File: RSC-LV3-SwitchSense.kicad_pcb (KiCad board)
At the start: 2 copper layers, 138 parts, among them J10 Molex 43045-0400, J11 Molex 43045-0400, J12 Molex 43045-0400, J13 Molex 43045-0400, J14 Molex 43045-0400, J15 Molex 43045-0400, J16 Molex 43045-0400, J17 Molex 43045-0400, J18 Molex 43045-0400, J2 USB_C_Receptacle_USB2.0_16P, J3 Conn_01x01, J5 Molex 43650-0500, J6 Molex 43650-0500, J8 FTSH-105-01-L-DV-K-A, J9 Molex 43045-0400, Q10 AO3400A, Q11 AO3400A, Q2 AO3400A, Q3 AO3400A, Q4 AO3400A, Q5 AO3400A, Q6 AO3400A, Q7 AO3400A, Q8 AO3400A, Q9 AO3400A, U1 STM32G0B1CBTx, U2 TJA1051T-3, U3 TPS54302, U5 TLV74033PDBVR, Y1 Crystal_GND24

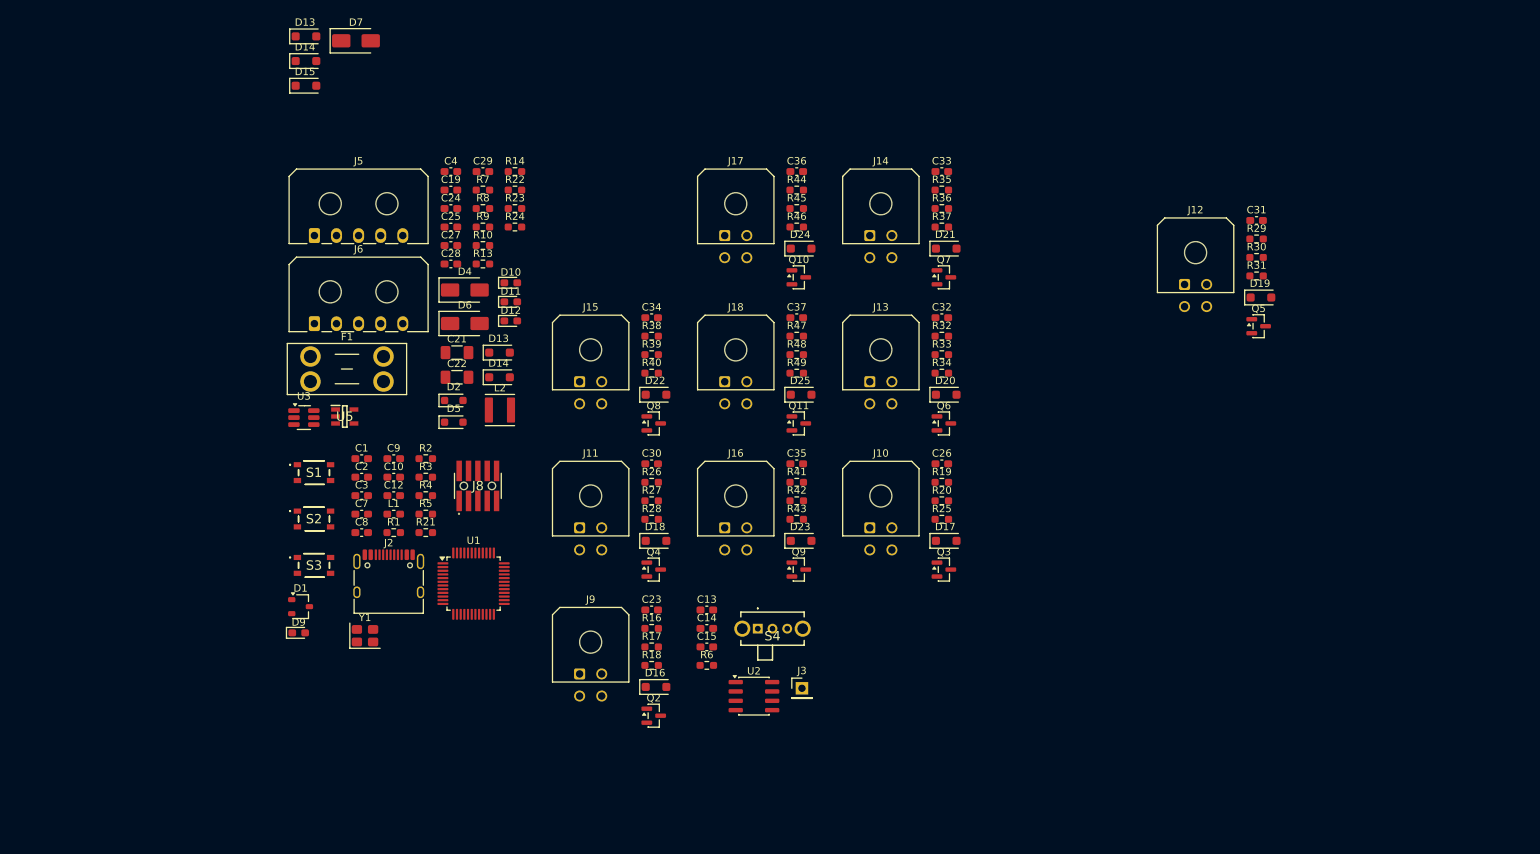
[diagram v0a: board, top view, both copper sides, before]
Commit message: updated pinout, begin layout
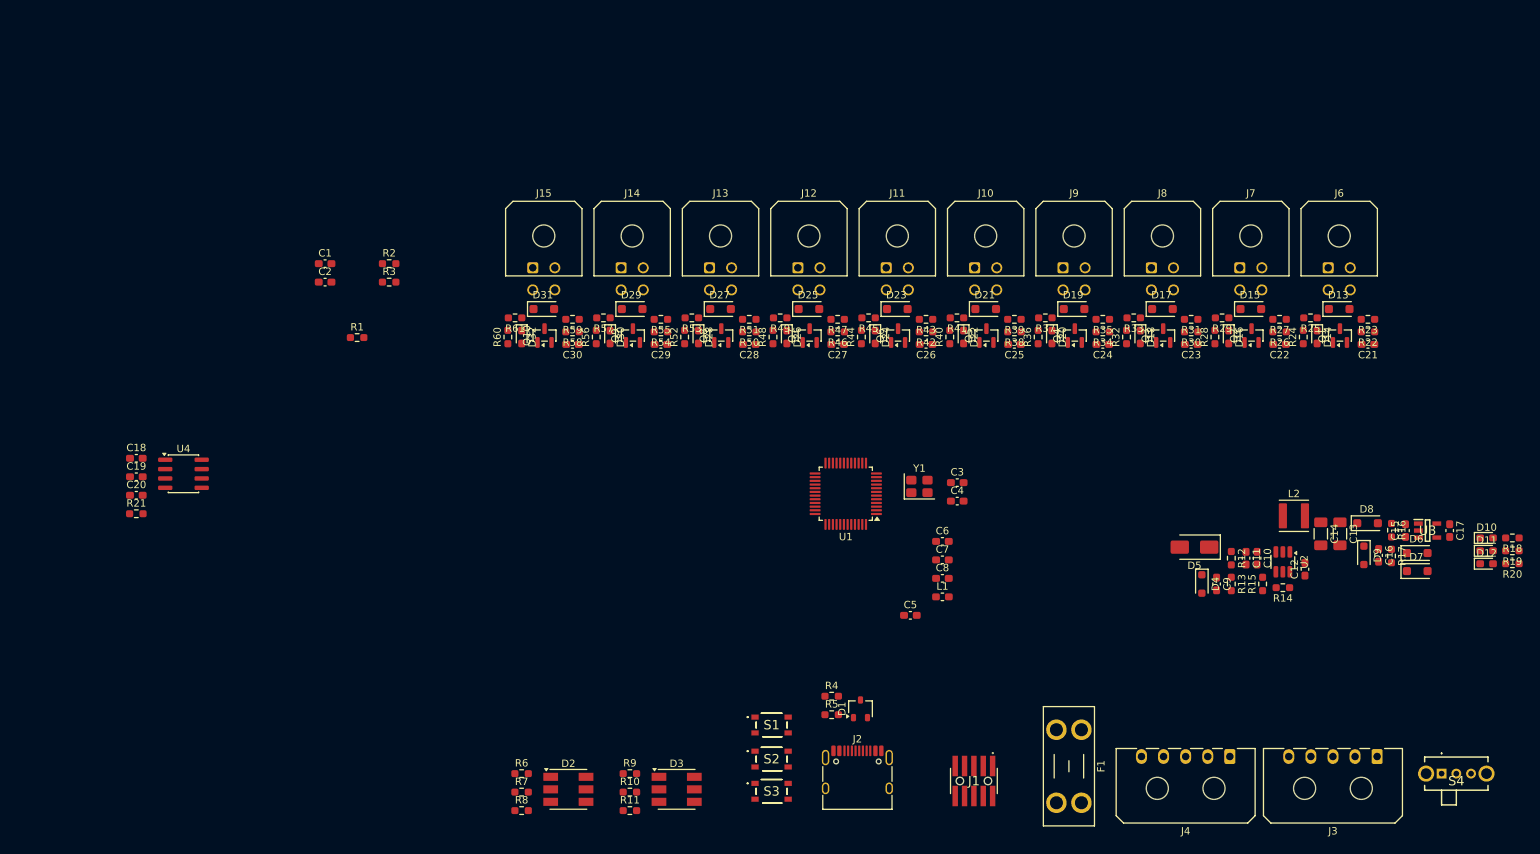
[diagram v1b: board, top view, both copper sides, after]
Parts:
- removed the C21 at (128.2, 75.8)
- removed the C22 at (128.2, 79.2)
- removed the C24 at (127.4, 56.3)
- removed the C25 at (127.4, 58.8)
- removed the C27 at (127.4, 61.3)
- removed the C28 at (127.4, 63.8)
- removed the C29 at (131.7, 51.3)
- removed the D13 at (134.0, 75.8)
- removed the D13 at (107.7, 32.9)
- removed the D14 at (107.7, 36.2)
- removed the D14 at (134.0, 79.2)
- removed the D15 at (107.7, 39.6)
- removed the J3 at (175.1, 121.4)
- removed the R22 at (136.1, 53.8)
- removed the R23 at (136.1, 56.3)
- removed the R24 at (136.1, 58.8)
- removed U5: TLV74033PDBVR, SamacSys_Parts:SOT95P280X145-5N
- added C11: 2.2u, Capacitor_SMD:C_0603_1608Metric_Pad1.08x0.95mm_HandSolder, F.Cu at (235.3, 103.8)
- added C16: 100n, Capacitor_SMD:C_0603_1608Metric_Pad1.08x0.95mm_HandSolder, F.Cu at (253.3, 103.4)
- added C17: 1u, Capacitor_SMD:C_0603_1608Metric_Pad1.08x0.95mm_HandSolder, F.Cu at (263.0, 100.0)
- added C18: 100n, Capacitor_SMD:C_0603_1608Metric_Pad1.08x0.95mm_HandSolder, F.Cu at (84.7, 90.2)
- added C20: 1u, Capacitor_SMD:C_0603_1608Metric_Pad1.08x0.95mm_HandSolder, F.Cu at (84.7, 95.2)
- added C5: 100n, Capacitor_SMD:C_0603_1608Metric_Pad1.08x0.95mm_HandSolder, F.Cu at (189.8, 111.5)
- added C6: 1u, Capacitor_SMD:C_0603_1608Metric_Pad1.08x0.95mm_HandSolder, F.Cu at (194.1, 101.5)
- added D14: LED, LED_SMD:LED_0603_1608Metric_Pad1.05x0.95mm_HandSolder, F.Cu at (245.0, 73.7)
- added D16: LED, LED_SMD:LED_0603_1608Metric_Pad1.05x0.95mm_HandSolder, F.Cu at (233.0, 73.7)
- added D18: LED, LED_SMD:LED_0603_1608Metric_Pad1.05x0.95mm_HandSolder, F.Cu at (221.0, 73.7)
- added D20: LED, LED_SMD:LED_0603_1608Metric_Pad1.05x0.95mm_HandSolder, F.Cu at (209.0, 73.7)
- added D22: LED, LED_SMD:LED_0603_1608Metric_Pad1.05x0.95mm_HandSolder, F.Cu at (197.0, 73.7)
- added D24: LED, LED_SMD:LED_0603_1608Metric_Pad1.05x0.95mm_HandSolder, F.Cu at (185.0, 73.7)
- added D26: LED, LED_SMD:LED_0603_1608Metric_Pad1.05x0.95mm_HandSolder, F.Cu at (173.0, 73.7)
- added D28: LED, LED_SMD:LED_0603_1608Metric_Pad1.05x0.95mm_HandSolder, F.Cu at (161.0, 73.7)
- added D3: LED_RGB, LED_SMD:LED_RGB_5050-6, F.Cu at (158.0, 135.1)
- added D30: LED, LED_SMD:LED_0603_1608Metric_Pad1.05x0.95mm_HandSolder, F.Cu at (149.0, 73.7)
- added D32: LED, LED_SMD:LED_0603_1608Metric_Pad1.05x0.95mm_HandSolder, F.Cu at (137.0, 73.7)
- added D8: D_Schottky, Diode_SMD:D_SOD-123F, F.Cu at (251.8, 99.0)
- added R11: 120, Resistor_SMD:R_0603_1608Metric_Pad0.98x0.95mm_HandSolder, F.Cu at (151.7, 138.0)
- added R12: 100k, Resistor_SMD:R_0603_1608Metric_Pad0.98x0.95mm_HandSolder, F.Cu at (233.3, 103.8)
- added R15: 12.7k, Resistor_SMD:R_0603_1608Metric_Pad0.98x0.95mm_HandSolder, F.Cu at (237.6, 107.2)
- added R16: 100k, Resistor_SMD:R_0603_1608Metric_Pad0.98x0.95mm_HandSolder, F.Cu at (255.1, 100.0)
- added R17: 100k, Resistor_SMD:R_0603_1608Metric_Pad0.98x0.95mm_HandSolder, F.Cu at (255.1, 103.5)
- added R18: 2.2k, Resistor_SMD:R_0603_1608Metric_Pad0.98x0.95mm_HandSolder, F.Cu at (271.5, 101.0)
- added R19: 470, Resistor_SMD:R_0603_1608Metric_Pad0.98x0.95mm_HandSolder, F.Cu at (271.5, 102.8)
- added R20: 120, Resistor_SMD:R_0603_1608Metric_Pad0.98x0.95mm_HandSolder, F.Cu at (271.5, 104.5)
- added R25: 470, Resistor_SMD:R_0603_1608Metric_Pad0.98x0.95mm_HandSolder, F.Cu at (244.1, 71.1)
- added R29: 470, Resistor_SMD:R_0603_1608Metric_Pad0.98x0.95mm_HandSolder, F.Cu at (232.1, 71.1)
- added R33: 470, Resistor_SMD:R_0603_1608Metric_Pad0.98x0.95mm_HandSolder, F.Cu at (220.1, 71.1)
- added R37: 470, Resistor_SMD:R_0603_1608Metric_Pad0.98x0.95mm_HandSolder, F.Cu at (208.1, 71.1)
- added R41: 470, Resistor_SMD:R_0603_1608Metric_Pad0.98x0.95mm_HandSolder, F.Cu at (196.1, 71.1)
- added R45: 470, Resistor_SMD:R_0603_1608Metric_Pad0.98x0.95mm_HandSolder, F.Cu at (184.1, 71.1)
- added R49: 470, Resistor_SMD:R_0603_1608Metric_Pad0.98x0.95mm_HandSolder, F.Cu at (172.1, 71.1)
- added R53: 470, Resistor_SMD:R_0603_1608Metric_Pad0.98x0.95mm_HandSolder, F.Cu at (160.1, 71.1)
- added R57: 470, Resistor_SMD:R_0603_1608Metric_Pad0.98x0.95mm_HandSolder, F.Cu at (148.1, 71.1)
- added R61: 470, Resistor_SMD:R_0603_1608Metric_Pad0.98x0.95mm_HandSolder, F.Cu at (136.1, 71.1)
- added U4: TJA1051T-3, Package_SO:SOIC-8_3.9x4.9mm_P1.27mm, F.Cu at (91.1, 92.3)
- C1, C2: value 6.8p -> 100n
- C10: value 100n -> 2.2u
- C13: value 100n -> 22u; footprint Capacitor_SMD:C_0603_1608Metric_Pad1.08x0.95mm_HandSolder -> Capacitor_SMD:C_1206_3216Metric_Pad1.33x1.80mm_HandSolder
- C14: value 1u -> 22u; footprint Capacitor_SMD:C_0603_1608Metric_Pad1.08x0.95mm_HandSolder -> Capacitor_SMD:C_1206_3216Metric_Pad1.33x1.80mm_HandSolder
- C15: value 100n -> 1u
- C3, C4: value 100n -> 6.8p
- C8: value 1u -> 100n
- D2: value D_Zener -> LED_RGB; footprint Diode_SMD:D_SOD-323_HandSoldering -> LED_SMD:LED_RGB_5050-6
- D4: value D_Schottky -> D_Zener; footprint Diode_SMD:D_SMA -> Diode_SMD:D_SOD-323_HandSoldering
- D5: value D_Zener -> D_Schottky; footprint Diode_SMD:D_SOD-323_HandSoldering -> Diode_SMD:D_SMA
- D6, D7: footprint Diode_SMD:D_SMA -> Diode_SMD:D_SOD-123F
- D9: value LED -> D_Zener; footprint LED_SMD:LED_0603_1608Metric_Pad1.05x0.95mm_HandSolder -> Diode_SMD:D_SOD-323_HandSoldering
- R10: value 5.1k -> 50
- R13: value 100k -> 5.1k
- R21: value 470 -> 120
- R6: value 120 -> 50
- R7, R9: value 100k -> 50
- R8: value 12.7k -> 120
- U2: value TJA1051T-3 -> TPS54302; footprint Package_SO:SOIC-8_3.9x4.9mm_P1.27mm -> Package_TO_SOT_SMD:SOT-23-6_Handsoldering
- U3: value TPS54302 -> TLV74033PDBVR; footprint Package_TO_SOT_SMD:SOT-23-6_Handsoldering -> SamacSys_Parts:SOT95P280X145-5N
- moved D7 161.1 mm to (258.6, 105.5)
- moved J3 160.7 mm to (253.2, 130.7), turned to 180 degrees
- moved U3 153.3 mm to (260.0, 100.0)
- moved D9 145.0 mm to (251.3, 103.4), turned to -90 degrees
- moved J4 137.5 mm to (233.2, 130.7), turned to 180 degrees
- moved D10 136.9 mm to (268.0, 101.0)
- moved D11 136.7 mm to (268.0, 102.8)
- moved D12 136.5 mm to (268.0, 104.5)
- moved D6 133.0 mm to (258.6, 103.0)
- moved C12 124.1 mm to (243.3, 105.2), turned to 90 degrees
- moved R14 118.6 mm to (240.3, 107.8), turned to 180 degrees
- moved C10 117.7 mm to (236.8, 103.8), turned to -90 degrees
- moved F1 116.3 mm to (213.0, 127.0), turned to -90 degrees
- moved J6 115.6 mm to (246.5, 64.3)
- moved C9 113.0 mm to (231.3, 107.2), turned to -90 degrees
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- renumbered C23 to C21, C26 to C22, C30 to C23, C31 to C24, C32 to C25, C33 to C26, C34 to C27, C35 to C28, C36 to C29, C37 to C30, D16 to D13, D17 to D15, D18 to D17, D20 to D21, D21 to D23, D22 to D25, D23 to D27, D24 to D29, D25 to D31, J8 to J1, J13 to J10, J14 to J11, J15 to J12, J16 to J13, J17 to J14, J18 to J15, J5 to J3, J6 to J4, J9 to J6, J10 to J7, J11 to J8, J12 to J9, Q2 to Q1, Q11 to Q10, Q3 to Q2, Q4 to Q3, Q5 to Q4, Q6 to Q5, Q7 to Q6, Q8 to Q7, Q9 to Q8, Q10 to Q9, R16 to R22, R17 to R23, R18 to R24, R19 to R26, R20 to R27, R25 to R28, R26 to R30, R27 to R31, R28 to R32, R29 to R34, R30 to R35, R31 to R36, R32 to R38, R33 to R39, R34 to R40, R35 to R42, R36 to R43, R37 to R44, R38 to R46, R39 to R47, R40 to R48, R41 to R50, R42 to R51, R43 to R52, R44 to R54, R45 to R55, R46 to R56, R47 to R58, R48 to R59, R49 to R60
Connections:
- C1 pad 1: HSE_IN -> BTN_USR1
- C10 pad 1: NRST -> +12V
- C12 pad 1: BTN_USR1 -> Net-(U2-BOOT)
- C12 pad 2: GND -> Net-(U2-SW)
- C13 pad 1: +5V -> +5V_BUCK
- C14 pad 1: +5V -> +5V_BUCK
- C15 pad 1: +3.3V -> +5V
- C19 pad 1: V_SENSE_12 -> +5V
- C2 pad 1: HSE_OUT -> NRST
- C21 pad 1: /Inputs/SwitchSense 1/SW_SENSE -> IN_1
- C22 pad 1: /Inputs/SwitchSense 2/SW_SENSE -> IN_2
- C23 pad 1: /Inputs/SwitchSense 3/SW_SENSE -> IN_3
- C24 pad 1: /Inputs/SwitchSense 4/SW_SENSE -> IN_4
- C25 pad 1: /Inputs/SwitchSense 5/SW_SENSE -> IN_5
- C26 pad 1: /Inputs/SwitchSense 6/SW_SENSE -> IN_6
- C27 pad 1: /Inputs/SwitchSense 7/SW_SENSE -> IN_7
- C28 pad 1: /Inputs/SwitchSense 8/SW_SENSE -> IN_8
- C29 pad 1: /Inputs/SwitchSense 9/SW_SENSE -> IN_9
- C3 pad 1: +3.3V -> HSE_IN
- C30 pad 1: /Inputs/SwitchSense 10/SW_SENSE -> IN_10
- C4 pad 1: Net-(U3-BOOT) -> HSE_OUT
- C4 pad 2: Net-(U3-SW) -> GND
- C7 pad 1: +3.3V -> +VDDA
- C9 pad 1: +VDDA -> V_SENSE_12
- D2 pad 1: V_SENSE_12 -> Net-(D2-RK)
- D2 pad 2: GND -> Net-(D2-GK)
- D4 pad 1: +5V -> V_SENSE_12
- D4 pad 2: +5V_USB -> GND
- D5 pad 1: V_SENSE_5 -> +12V
- D5 pad 2: GND -> Net-(D5-A)
- D6 pad 2: +5V_BUS -> +5V_USB
- D7 pad 1: Net-(D7-K) -> +5V
- D7 pad 2: +12V -> +5V_BUS
- D9 pad 1: GND -> V_SENSE_5
- D9 pad 2: Net-(D9-A) -> GND
- F1 pad 2: +12V -> Net-(D5-A)
- L2 pad 1: Net-(U3-SW) -> Net-(U2-SW)
- Q1 pad 1: /Inputs/SwitchSense 1/FET_EN -> OUT_1
- Q10 pad 1: /Inputs/SwitchSense 10/FET_EN -> OUT_10
- Q2 pad 1: /Inputs/SwitchSense 2/FET_EN -> OUT_2
- Q3 pad 1: /Inputs/SwitchSense 3/FET_EN -> OUT_3
- Q4 pad 1: /Inputs/SwitchSense 4/FET_EN -> OUT_4
- Q5 pad 1: /Inputs/SwitchSense 5/FET_EN -> OUT_5
- Q6 pad 1: /Inputs/SwitchSense 6/FET_EN -> OUT_6
- Q7 pad 1: /Inputs/SwitchSense 7/FET_EN -> OUT_7
- Q8 pad 1: /Inputs/SwitchSense 8/FET_EN -> OUT_8
- Q9 pad 1: /Inputs/SwitchSense 9/FET_EN -> OUT_9
- R10 pad 1: V_SENSE_12 -> GND
- R10 pad 2: GND -> Net-(D3-GK)
- R13 pad 1: +5V -> V_SENSE_12
- R13 pad 2: V_SENSE_5 -> GND
- R14 pad 1: V_SENSE_5 -> +5V_BUCK
- R14 pad 2: GND -> Net-(U2-FB)
- R21 pad 1: LED_USR -> PRIMARY_CAN+
- R21 pad 2: Net-(D9-A) -> Net-(S4-NO)
- R22 pad 1: /Inputs/SwitchSense 1/SW_SENSE -> IN_1
- R24 pad 1: /Inputs/SwitchSense 1/FET_EN -> OUT_1
- R26 pad 1: /Inputs/SwitchSense 2/SW_SENSE -> IN_2
- R28 pad 1: /Inputs/SwitchSense 2/FET_EN -> OUT_2
- R3 pad 2: Net-(J2-CC1) -> BTN_USR1
- R30 pad 1: /Inputs/SwitchSense 3/SW_SENSE -> IN_3
- R32 pad 1: /Inputs/SwitchSense 3/FET_EN -> OUT_3
- R34 pad 1: /Inputs/SwitchSense 4/SW_SENSE -> IN_4
- R36 pad 1: /Inputs/SwitchSense 4/FET_EN -> OUT_4
- R38 pad 1: /Inputs/SwitchSense 5/SW_SENSE -> IN_5
- R4 pad 2: Net-(J2-CC2) -> Net-(J2-CC1)
- R40 pad 1: /Inputs/SwitchSense 5/FET_EN -> OUT_5
- R42 pad 1: /Inputs/SwitchSense 6/SW_SENSE -> IN_6
- R44 pad 1: /Inputs/SwitchSense 6/FET_EN -> OUT_6
- R46 pad 1: /Inputs/SwitchSense 7/SW_SENSE -> IN_7
- R48 pad 1: /Inputs/SwitchSense 7/FET_EN -> OUT_7
- R5 pad 2: BTN_USR1 -> Net-(J2-CC2)
- R50 pad 1: /Inputs/SwitchSense 8/SW_SENSE -> IN_8
- R52 pad 1: /Inputs/SwitchSense 8/FET_EN -> OUT_8
- R54 pad 1: /Inputs/SwitchSense 9/SW_SENSE -> IN_9
- R56 pad 1: /Inputs/SwitchSense 9/FET_EN -> OUT_9
- R58 pad 1: /Inputs/SwitchSense 10/SW_SENSE -> IN_10
- R6 pad 1: PRIMARY_CAN+ -> GND
- R6 pad 2: Net-(S4-NO) -> Net-(D2-BK)
- R60 pad 1: /Inputs/SwitchSense 10/FET_EN -> OUT_10
- R7 pad 1: +5V_BUCK -> GND
- R7 pad 2: Net-(U3-FB) -> Net-(D2-GK)
- R8 pad 1: Net-(U3-FB) -> GND
- R8 pad 2: GND -> Net-(D2-RK)
- R9 pad 1: +12V -> GND
- R9 pad 2: V_SENSE_12 -> Net-(D3-BK)
- U1 pad 11: unconnected-(U1-PA0-Pad11) -> V_SENSE_5
- U1 pad 12: unconnected-(U1-PA1-Pad12) -> V_SENSE_12
- U1 pad 13: unconnected-(U1-PA2-Pad13) -> IN_1
- U1 pad 14: unconnected-(U1-PA3-Pad14) -> IN_2
- U1 pad 15: unconnected-(U1-PA4-Pad15) -> IN_3
- U1 pad 16: LED_USR -> IN_4
- U1 pad 17: unconnected-(U1-PA6-Pad17) -> IN_5
- U1 pad 18: unconnected-(U1-PA7-Pad18) -> IN_6
- U1 pad 19: unconnected-(U1-PB0-Pad19) -> OUT_3
- U1 pad 20: unconnected-(U1-PB1-Pad20) -> OUT_4
- U1 pad 21: unconnected-(U1-PB2-Pad21) -> IN_7
- U1 pad 22: unconnected-(U1-PB10-Pad22) -> IN_8
- U1 pad 23: unconnected-(U1-PB11-Pad23) -> IN_9
- U1 pad 24: unconnected-(U1-PB12-Pad24) -> IN_10
- U1 pad 26: unconnected-(U1-PB14-Pad26) -> OUT_9
- U1 pad 27: unconnected-(U1-PB15-Pad27) -> OUT_10
- U1 pad 28: unconnected-(U1-PA8-Pad28) -> STAT0_R
- U1 pad 29: unconnected-(U1-PA9/UCPD1_DBCC1-Pad29) -> STAT0_G
- U1 pad 30: unconnected-(U1-PC6-Pad30) -> STAT1_B
- U1 pad 32: unconnected-(U1-PA10/UCPD1_DBCC2-Pad32) -> STAT0_B
- U1 pad 37: unconnected-(U1-PA15-Pad37) -> STAT1_R
- U1 pad 42: unconnected-(U1-PB3-Pad42) -> STAT1_G
- U1 pad 43: unconnected-(U1-PB4-Pad43) -> OUT_1
- U1 pad 44: unconnected-(U1-PB5-Pad44) -> OUT_2
- U1 pad 45: unconnected-(U1-PB6-Pad45) -> OUT_5
- U1 pad 46: unconnected-(U1-PB7-Pad46) -> OUT_6
- U1 pad 47: unconnected-(U1-PB8-Pad47) -> OUT_7
- U1 pad 48: unconnected-(U1-PB9-Pad48) -> OUT_8
- U2 pad 1: FDCAN1_TX -> GND
- U2 pad 2: GND -> Net-(U2-SW)
- U2 pad 3: +5V -> +12V
- U2 pad 4: FDCAN1_RX -> Net-(U2-FB)
- U2 pad 5: +3.3V -> unconnected-(U2-EN-Pad5)
- U2 pad 6: PRIMARY_CAN- -> Net-(U2-BOOT)
- U3 pad 1: GND -> +5V
- U3 pad 2: Net-(U3-SW) -> GND
- U3 pad 3: Net-(D7-K) -> +5V
- U3 pad 4: Net-(U3-FB) -> unconnected-(U3-NC-Pad4)
- U3 pad 5: unconnected-(U3-EN-Pad5) -> +3.3V

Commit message: more layout work
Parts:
- moved C17 110.4 mm to (152.7, 95.5), turned to 90 degrees
- moved U3 104.4 mm to (155.7, 95.5), turned to 180 degrees
- moved C15 98.5 mm to (158.7, 95.5), turned to -90 degrees
- moved R17 95.2 mm to (160.6, 92.0), turned to 90 degrees
- moved D7 94.8 mm to (164.0, 99.2), turned to 180 degrees
- moved R16 94.7 mm to (160.6, 95.5), turned to 90 degrees
- moved D6 94.6 mm to (164.0, 101.7), turned to 180 degrees
- moved D5 93.6 mm to (135.0, 109.5)
- moved C16 91.7 mm to (162.3, 92.1), turned to 90 degrees
- moved S3 88.3 mm to (83.0, 127.0)
- moved D8 87.9 mm to (164.0, 96.7), turned to 180 degrees
- moved D9 87.8 mm to (164.3, 92.1), turned to 90 degrees
- moved D3 81.8 mm to (83.5, 101.5)
- moved R10 81.8 mm to (77.2, 101.9)
- moved R11 81.8 mm to (77.2, 104.4)
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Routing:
- net GND: track 0.00 -> 150.3 mm
- net +12V: track 0.00 -> 88.5 mm
- net Net-(J15-Pin_2): track 0.00 -> 16.6 mm
- net Net-(J14-Pin_2): track 0.00 -> 16.6 mm
- net Net-(J13-Pin_2): track 0.00 -> 16.6 mm
- net Net-(J12-Pin_2): track 0.00 -> 16.6 mm
- net Net-(J9-Pin_2): track 0.00 -> 16.6 mm
- net Net-(J8-Pin_2): track 0.00 -> 16.6 mm
- net Net-(J7-Pin_2): track 0.00 -> 16.6 mm
- net Net-(J6-Pin_2): track 0.00 -> 16.6 mm
- net Net-(J11-Pin_2): track 0.00 -> 16.6 mm
- net Net-(J10-Pin_2): track 0.00 -> 16.6 mm
- net OUT_6: track 0.00 -> 13.6 mm
- net OUT_5: track 0.00 -> 13.6 mm
- net OUT_4: track 0.00 -> 13.6 mm
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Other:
- board outline added: 140 x 80 mm

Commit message: more work on layout
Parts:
- removed C8: 100n, Capacitor_SMD:C_0603_1608Metric_Pad1.08x0.95mm_HandSolder
- moved C2 36.8 mm to (136.6, 86.0)
- moved C1 26.6 mm to (131.0, 100.0)
- moved R1 25.7 mm to (136.6, 84.2)
- moved R3 18.0 mm to (131.0, 101.8), turned to 180 degrees
- moved L1 10.1 mm to (136.9, 95.0), turned to 180 degrees
- moved C5 8.24 mm to (137.8, 92.2), turned to 90 degrees
- moved R2 7.58 mm to (114.2, 93.8)
- moved Y1 6.50 mm to (140.8, 90.0), turned to 90 degrees
- moved C18 5.62 mm to (101.2, 94.0)
- moved C19 5.62 mm to (95.2, 90.5)
- moved C20 5.62 mm to (93.8, 90.5)
- moved R21 5.62 mm to (105.2, 90.0)
- moved U4 5.62 mm to (99.8, 90.5)
- moved R5 5.41 mm to (108.5, 110.2), turned to 180 degrees
- moved C4 5.27 mm to (140.8, 87.0)
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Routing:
- net GND: track 150.3 -> 154.1 mm
- net HSE_OUT: track 0.00 -> 1.91 mm
- net HSE_IN: track 0.00 -> 1.91 mm

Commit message: add second CAN and backup domain components
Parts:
- added C31: 6.8p, Capacitor_SMD:C_0603_1608Metric_Pad1.08x0.95mm_HandSolder, F.Cu at (135.1, 99.5)
- added C32: 100n, Capacitor_SMD:C_0603_1608Metric_Pad1.08x0.95mm_HandSolder, F.Cu at (97.5, 93.9)
- added C33: 100n, Capacitor_SMD:C_0603_1608Metric_Pad1.08x0.95mm_HandSolder, F.Cu at (106.3, 97.7)
- added C34: 1u, Capacitor_SMD:C_0603_1608Metric_Pad1.08x0.95mm_HandSolder, F.Cu at (108.0, 97.7)
- added C8: 6.8p, Capacitor_SMD:C_0603_1608Metric_Pad1.08x0.95mm_HandSolder, F.Cu at (135.1, 105.5)
- added J16: Molex 43650-0200, Connector_Molex:Molex_Micro-Fit_3.0_43650-0200_1x02_P3.00mm_Horizontal, F.Cu at (79.8, 88.0)
- added J5: Molex 43650-0200, Connector_Molex:Molex_Micro-Fit_3.0_43650-0200_1x02_P3.00mm_Horizontal, F.Cu at (79.8, 99.0)
- added R62: 120, Resistor_SMD:R_0603_1608Metric_Pad0.98x0.95mm_HandSolder, F.Cu at (95.8, 98.2)
- added S5: SLW-864587-2A-RA-N-D, SamacSys_Parts:SLW8645872ARAND, F.Cu at (77.5, 108.5)
- added U5: TJA1051T-3, Package_SO:SOIC-8_3.9x4.9mm_P1.27mm, F.Cu at (101.5, 97.6)
- added Y2: 32.768 kHz 6pF, Crystal:Crystal_C26-LF_D2.1mm_L6.5mm_Horizontal, F.Cu at (134.2, 103.5)
- moved F1 56.3 mm to (197.8, 112.0), turned to 90 degrees
- moved C20 55.1 mm to (147.5, 102.6), turned to 0 degrees
- moved C19 54.0 mm to (147.5, 104.1), turned to 0 degrees
- moved U4 51.1 mm to (147.5, 108.6), turned to -90 degrees
- moved R21 49.1 mm to (148.0, 114.1), turned to -90 degrees
- moved C18 45.7 mm to (144.0, 110.1), turned to 90 degrees
- moved D2 35.6 mm to (99.0, 123.4)
- moved R11 33.8 mm to (109.5, 114.1), turned to 90 degrees
- moved D3 33.5 mm to (99.2, 131.1)
- moved R10 32.2 mm to (107.0, 114.1), turned to 90 degrees
- moved R9 31.0 mm to (104.5, 114.1), turned to 90 degrees
- moved R6 29.6 mm to (94.2, 113.6), turned to 90 degrees
- moved R7 29.2 mm to (96.7, 113.6), turned to 90 degrees
- moved R8 29.1 mm to (99.2, 113.6), turned to 90 degrees
- moved R20 23.5 mm to (201.0, 84.1), turned to -90 degrees
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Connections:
- U1 pad 2: unconnected-(U1-PC14-Pad2) -> LSE_IN
- U1 pad 3: unconnected-(U1-PC15-Pad3) -> LSE_OUT
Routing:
- net AUX_CAN-: track 0.00 -> 14.4 mm, vias 0 -> 1
- net AUX_CAN+: track 0.00 -> 13.4 mm, vias 0 -> 1
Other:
- board size 140 x 80 mm -> 140 x 85 mm
- board text added: "BOOT"
- board text added: "NRST"
- board text added: "USR"
